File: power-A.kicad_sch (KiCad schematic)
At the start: 30 parts, among them J201 PCB Receptacle, J202 PCB Receptacle, J203 Conn_01x06, U201 AMS1117-ADJ_SOT223

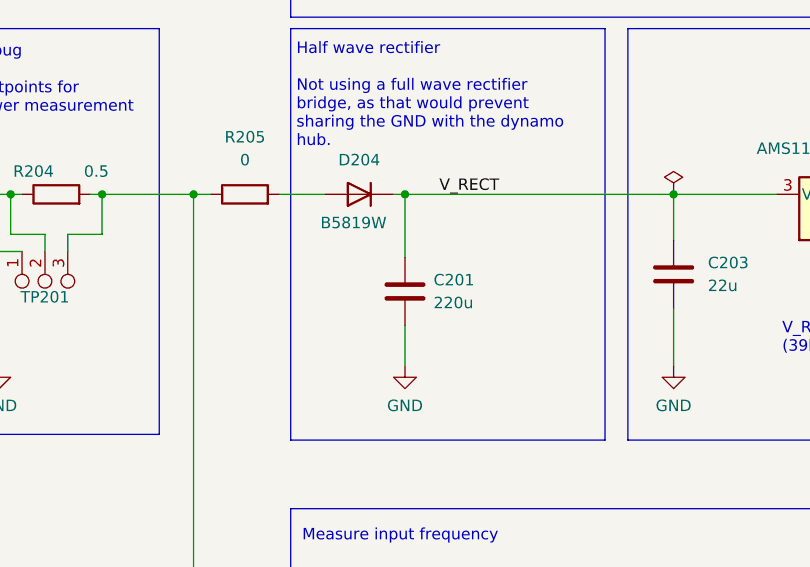
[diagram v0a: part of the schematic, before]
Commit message: exchange C to polarized
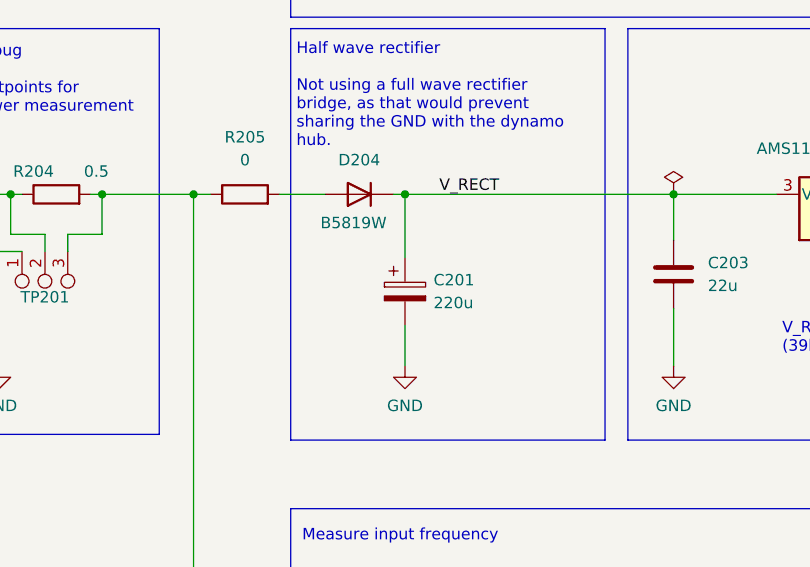
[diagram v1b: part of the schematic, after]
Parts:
- C201: symbol Device:C -> Device:C_Polarized
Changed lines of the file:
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@@
     (pin "1")
   )
-  (symbol (lib_id "Device:C") (at 139.7 91.44 0) (unit 1)
+  (symbol (lib_id "Device:C_Polarized") (at 139.7 91.44 0) (unit 1)
     (in_bom yes) (on_board yes)
     (property "Reference" "C201" (id 0) (at 142.875 90.17 0)

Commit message: update power indicator LED to match JLC coponent
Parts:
- D207: footprint LED_SMD:LED_0805_2012Metric -> LED_SMD:LED_0603_1608Metric
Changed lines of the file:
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@@
       (effects (font (size 1.27 1.27)) (justify right))
     )
-    (property "Footprint" "LED_SMD:LED_0805_2012Metric" (id 2) (at 255.27 92.075 0)
+    (property "Footprint" "LED_SMD:LED_0603_1608Metric" (id 2) (at 255.27 92.075 0)
       (effects (font (size 1.27 1.27)) hide)
     )
